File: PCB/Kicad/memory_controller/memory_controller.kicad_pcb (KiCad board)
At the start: 6 copper layers, 150 x 100 mm, 119 parts, among them U1 74245, U10 74283, U11 74377, U12 74377, U13 74245, U14 74245, U15 74245, U16 74245, U17 74245, U18 74245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

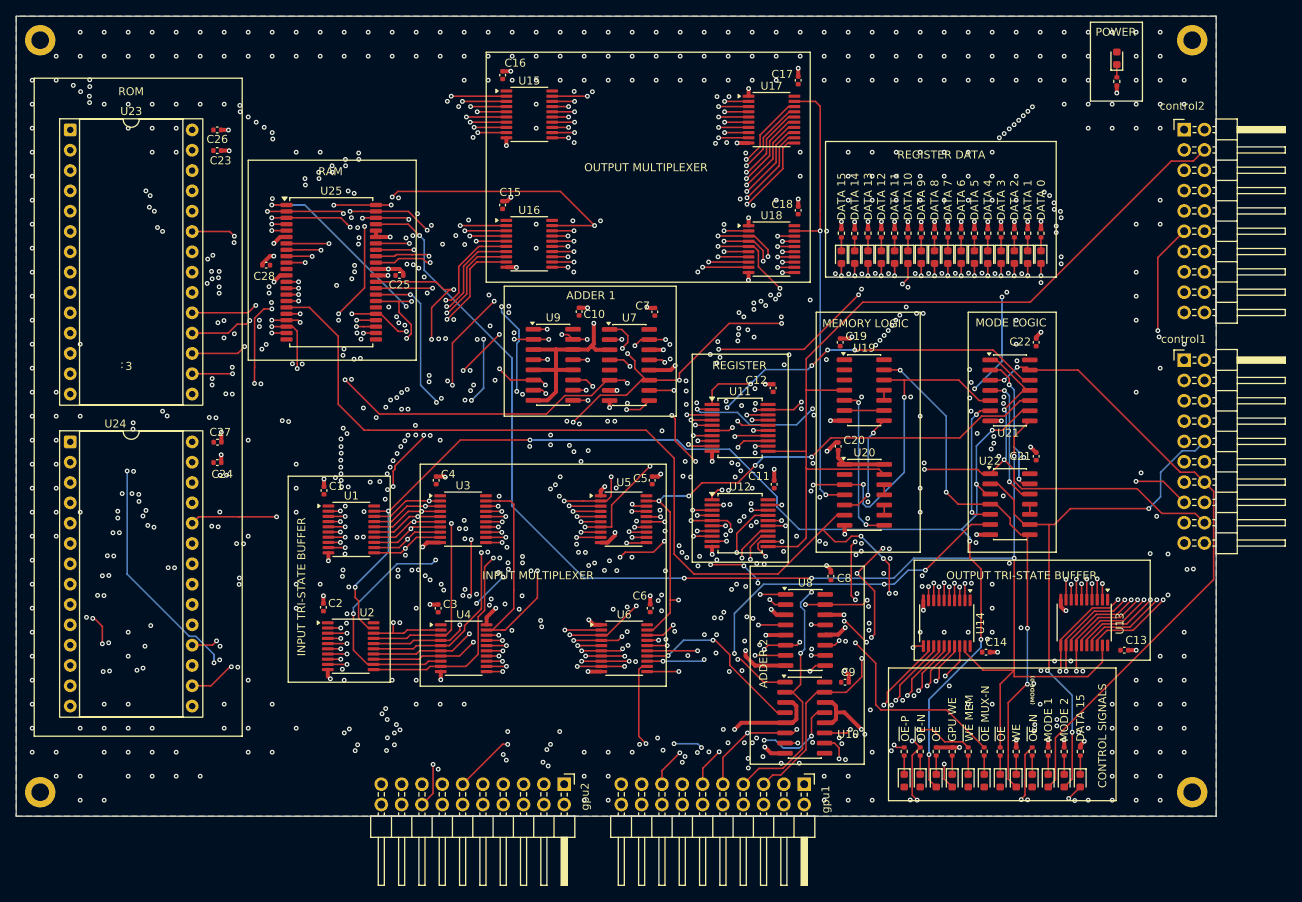
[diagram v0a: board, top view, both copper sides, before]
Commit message: silkscreen fix
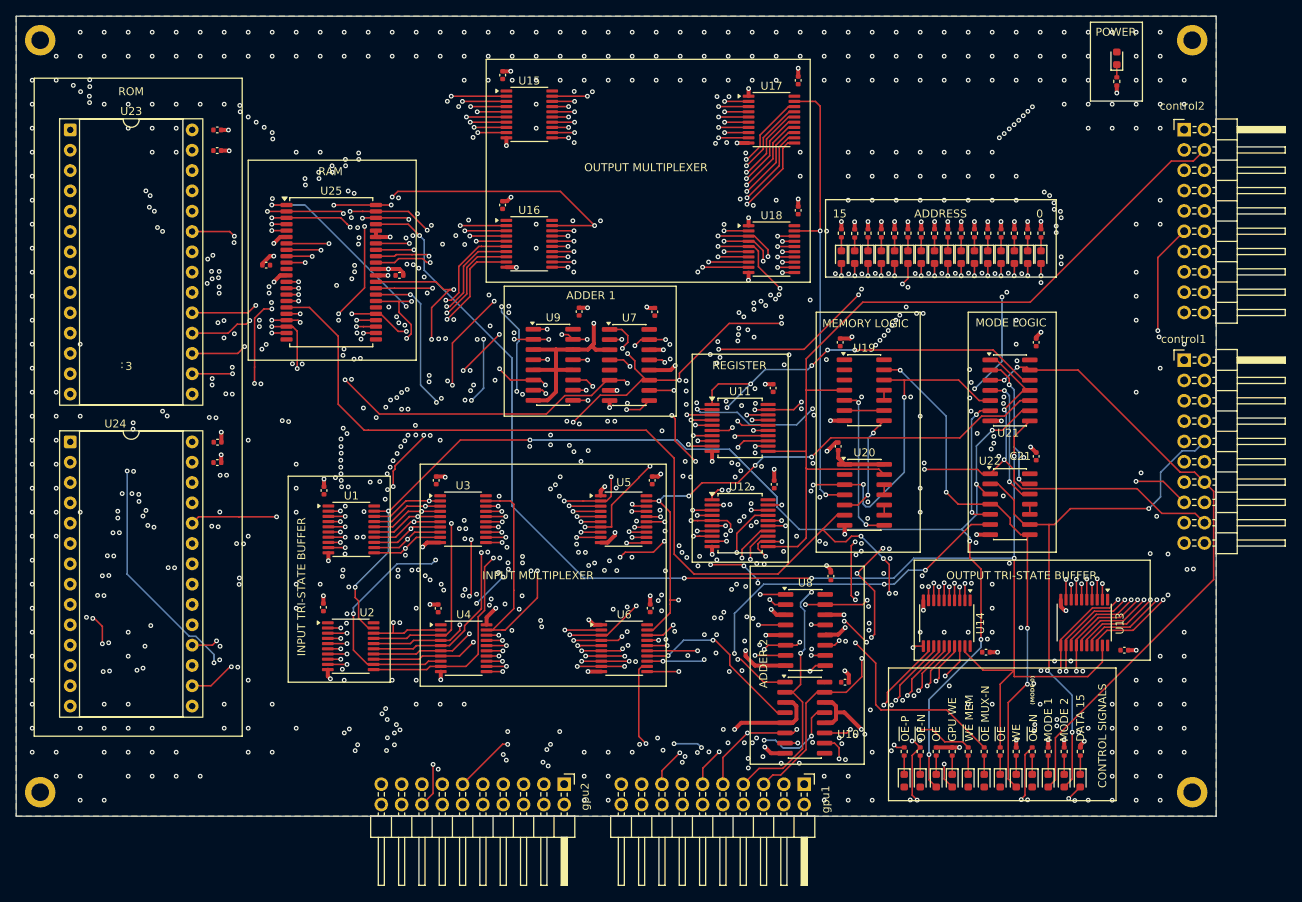
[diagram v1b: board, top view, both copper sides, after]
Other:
- board text added: "0"
- board text added: "15"
- board text added: "ADDRESS"
- board text removed: "DATA 0"
- board text removed: "DATA 1"
- board text removed: "DATA 10"
- board text removed: "DATA 11"
- board text removed: "DATA 12"
- board text removed: "DATA 13"
- board text removed: "DATA 14"
- board text removed: "DATA 2"
- board text removed: "DATA 3"
- board text removed: "DATA 4"
- board text removed: "DATA 5"
- board text removed: "DATA 6"
- board text removed: "DATA 7"
- board text removed: "DATA 8"
- board text removed: "DATA 9"
- board text removed: "REGISTER DATA"
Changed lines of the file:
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@@
 			(at -0.77 -2 180)
 			(layer "F.SilkS")
+			(hide yes)
 			(effects
 				(font
@@
 			(at 0.324 -1.885 180)
 			(layer "F.SilkS")
+			(hide yes)
 			(effects
 				(font
@@
 			(at 0 -1.16 0)
 			(layer "F.SilkS")
+			(hide yes)
 			(effects
 				(font
@@
 			(at -0.25 1.38 0)
 			(layer "F.SilkS")
+			(hide yes)
 			(effects
 				(font
@@
 			(at -0.75 1.524 180)
 			(layer "F.SilkS")
+			(hide yes)
 			(effects
 				(font
@@
 			(at -0.77 -2 180)
 			(layer "F.SilkS")
+			(hide yes)
 			(effects
 				(font
@@
 			(at 0.255 -1.6638 180)
 			(layer "F.SilkS")
+			(hide yes)
 			(effects
 				(font
@@
 			(at 0 -1.16 0)
 			(layer "F.SilkS")
+			(hide yes)
 			(effects
 				(font
@@
 			(at -0.42 -1.255 0)
 			(layer "F.SilkS")
+			(hide yes)
 			(effects
 				(font
@@
 			(at -0.52 -1.5 180)
 			(layer "F.SilkS")
+			(hide yes)
 			(effects
 				(font
@@
 			(at -0.77 2 0)
 			(layer "F.SilkS")
+			(hide yes)
 			(effects
 				(font
@@
 			(at -1.02 1.905 180)
 			(layer "F.SilkS")
+			(hide yes)
 			(effects
 				(font
@@
 			(at -0.4 1.25 180)
 			(layer "F.SilkS")
+			(hide yes)
 			(effects
 				(font
@@
 			(at -0.245 1.475 180)
 			(layer "F.SilkS")
+			(hide yes)
 			(effects
 				(font
@@
 			(at -0.603763 -1.455 0)
 			(layer "F.SilkS")
+			(hide yes)
 			(effects
 				(font
@@
 			(at -0.77 2 0)
 			(layer "F.SilkS")
+			(hide yes)
 			(effects
 				(font
@@
 			(at -0.33 1.25 0)
 			(layer "F.SilkS")
+			(hide yes)
 			(effects
 				(font
@@
 			(at -0.77 -1.5 180)
 			(layer "F.SilkS")
+			(hide yes)
 			(effects
 				(font
@@
 			(at -0.98 2.119071 180)
 			(layer "F.SilkS")
+			(hide yes)
 			(effects
 				(font
@@
 			(at -1.52 -1.567 0)
 			(layer "F.SilkS")
+			(hide yes)
 			(effects
 				(font
@@
 			(at -1.55 1.3 180)
 			(layer "F.SilkS")
+			(hide yes)
 			(effects
 				(font
@@
 			(at -0.07 2 180)
 			(layer "F.SilkS")
+			(hide yes)
 			(effects
 				(font
@@
 			(at -0.538 -1.5245 0)
 			(layer "F.SilkS")
+			(hide yes)
 			(effects
 				(font
@@
 			(at -1.48 1.25 180)
 			(layer "F.SilkS")
+			(hide yes)
 			(effects
 				(font
@@
 			(at -1.27 1.25 180)
 			(layer "F.SilkS")
+			(hide yes)
 			(effects
 				(font
@@
 			(at -1.606 -0.9545 0)
 			(layer "F.SilkS")
+			(hide yes)
 			(effects
 				(font
@@
 			(at -0.5 -1.5 0)
 			(layer "F.SilkS")
+			(hide yes)
 			(effects
 				(font
@@
 	)
 	(gr_rect
-		(start 188.75 74.5)
+		(start 188.75 75.39)
 		(end 229.25 103.25)
 		(stroke
@@
 	)
 	(gr_rect
-		(start 231.17 85.66)
+		(start 231.17 92.93)
 		(end 260 102.61)
 		(stroke
@@
 		)
 	)
-	(gr_text "REGISTER DATA"
-		(at 240.13 87.91 0)
-		(layer "F.SilkS")
-		(effects
-			(font
-				(size 1 1)
-				(thickness 0.15)
-			)
-			(justify left bottom)
-		)
-	)
-	(gr_text "OUTPUT TRI-STATE BUFFER"
-		(at 246.25 140.5 0)
+	(gr_text "15"
+		(at 232.070952 95.28 0)
 		(layer "F.SilkS")
 		(effects
@@
 		)
 	)
-	(gr_text "MODE LOGIC"
-		(at 249.9 108.9 0)
+	(gr_text "ADDRESS"
+		(at 242.24 95.28 0)
 		(layer "F.SilkS")
 		(effects
@@
 		)
 	)
-	(gr_text "POWER"
-		(at 264.905381 72.57 0)
-		(layer "F.SilkS")
-		(effects
-			(font
-				(size 1 1)
-				(thickness 0.15)
-			)
-			(justify left bottom)
-		)
-	)
-	(gr_text "INPUT TRI-STATE BUFFER"
-		(at 166.25 150 90)
-		(layer "F.SilkS")
-		(effects
-			(font
-				(size 1 1)
-				(thickness 0.15)
-			)
-			(justify left bottom)
-		)
-	)
-	(gr_text "ADDER 2"
-		(at 224 154 90)
+	(gr_text "OUTPUT TRI-STATE BUFFER"
+		(at 246.25 140.5 0)
 		(layer "F.SilkS")
 		(effects
@@
 		)
 	)
-	(gr_text "DATA 15"
-		(at 233.750083 95.51 90)
+	(gr_text "MODE LOGIC"
+		(at 249.9 108.9 0)
 		(layer "F.SilkS")
 		(effects
@@
 		)
 	)
-	(gr_text "DATA 14"
-		(at 235.413416 95.51 90)
+	(gr_text "0"
+		(at 257.497143 95.28 0)
 		(layer "F.SilkS")
 		(effects
@@
 		)
 	)
-	(gr_text "DATA 13"
-		(at 237.07675 95.51 90)
+	(gr_text "POWER"
+		(at 264.905381 72.57 0)
 		(layer "F.SilkS")
 		(effects
@@
 		)
 	)
-	(gr_text "DATA 12"
-		(at 238.740083 95.51 90)
+	(gr_text "INPUT TRI-STATE BUFFER"
+		(at 166.25 150 90)
 		(layer "F.SilkS")
 		(effects
@@
 		)
 	)
-	(gr_text "DATA 11"
-		(at 240.403416 95.51 90)
+	(gr_text "ADDER 2"
+		(at 224 154 90)
 		(layer "F.SilkS")
 		(effects
@@
 		)
 	)
-	(gr_text "DATA 10"
-		(at 242.06675 95.51 90)
-		(layer "F.SilkS")
-		(effects
-			(font
-				(size 1 1)
-				(thickness 0.15)
-			)
-			(justify left bottom)
-		)
-	)
 	(gr_text "~{OE}-N"
 		(at 243.722583 160.69 90)
@@
 		)
 	)
-	(gr_text "DATA 9"
-		(at 243.730083 95.51 90)
-		(layer "F.SilkS")
-		(effects
-			(font
-				(size 1 1)
-				(thickness 0.15)
-			)
-			(justify left bottom)
-		)
-	)
-	(gr_text "DATA 8"
-		(at 245.393416 95.51 90)
-		(layer "F.SilkS")
-		(effects
-			(font
-				(size 1 1)
-				(thickness 0.15)
-			)
-			(justify left bottom)
-		)
-	)
 	(gr_text "OE"
 		(at 245.60175 160.69 90)
@@
 		)
 	)
-	(gr_text "DATA 7"
-		(at 247.05675 95.51 90)
-		(layer "F.SilkS")
-		(effects
-			(font
-				(size 1 1)
-				(thickness 0.15)
-			)
-			(justify left bottom)
-		)
-	)
 	(gr_text "GPU WE"
 		(at 247.60175 160.69 90)
@@
 		)
 	)
-	(gr_text "DATA 6"
-		(at 248.720083 95.51 90)
-		(layer "F.SilkS")
-		(effects
-			(font
-				(size 1 1)
-				(thickness 0.15)
-			)
-			(justify left bottom)
-		)
-	)
 	(gr_text "~{WE} MEM"
 		(at 249.722583 160.69 90)
@@
 		)
 	)
-	(gr_text "DATA 5"
-		(at 250.383416 95.51 90)
-		(layer "F.SilkS")
-		(effects
-			(font
-				(size 1 1)
-				(thickness 0.15)
-			)
-			(justify left bottom)
-		)
-	)
 	(gr_text "~{OE} MUX-N"
 		(at 251.722583 160.69 90)
@@
 		)
 	)
-	(gr_text "DATA 4"
-		(at 252.04675 95.51 90)
-		(layer "F.SilkS")
-		(effects
-			(font
-				(size 1 1)
-				(thickness 0.15)
-			)
-			(justify left bottom)
-		)
-	)
-	(gr_text "DATA 3"
-		(at 253.710083 95.51 90)
-		(layer "F.SilkS")
-		(effects
-			(font
-				(size 1 1)
-				(thickness 0.15)
-			)
-			(justify left bottom)
-		)
-	)
 	(gr_text "~{OE}"
 		(at 253.722583 160.69 90)
@@
 		)
 	)
-	(gr_text "DATA 2"
-		(at 255.373416 95.51 90)
-		(layer "F.SilkS")
-		(effects
-			(font
-				(size 1 1)
-				(thickness 0.15)
-			)
-			(justify left bottom)
-		)
-	)
 	(gr_text "WE"
 		(at 255.60175 160.69 90)
@@
 		)
 	)
-	(gr_text "DATA 1"
-		(at 257.03675 95.51 90)
-		(layer "F.SilkS")
-		(effects
-			(font
-				(size 1 1)
-				(thickness 0.15)
-			)
-			(justify left bottom)
-		)
-	)
 	(gr_text "~{OE}-N"
 		(at 257.722583 160.69 90)
 		(layer "F.SilkS")
 		(effects
-			(font
-				(size 1 1)
-				(thickness 0.15)
-			)
-			(justify left bottom)
-		)
-	)
-	(gr_text "DATA 0"
-		(at 258.700083 95.51 90)
-		(layer "F.SilkS")
-		(effects
